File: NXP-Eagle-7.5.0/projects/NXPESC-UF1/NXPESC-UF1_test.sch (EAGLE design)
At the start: 2 parts, among them U1 MKV31F512VLL12-M, U2 MC34GD3000EP

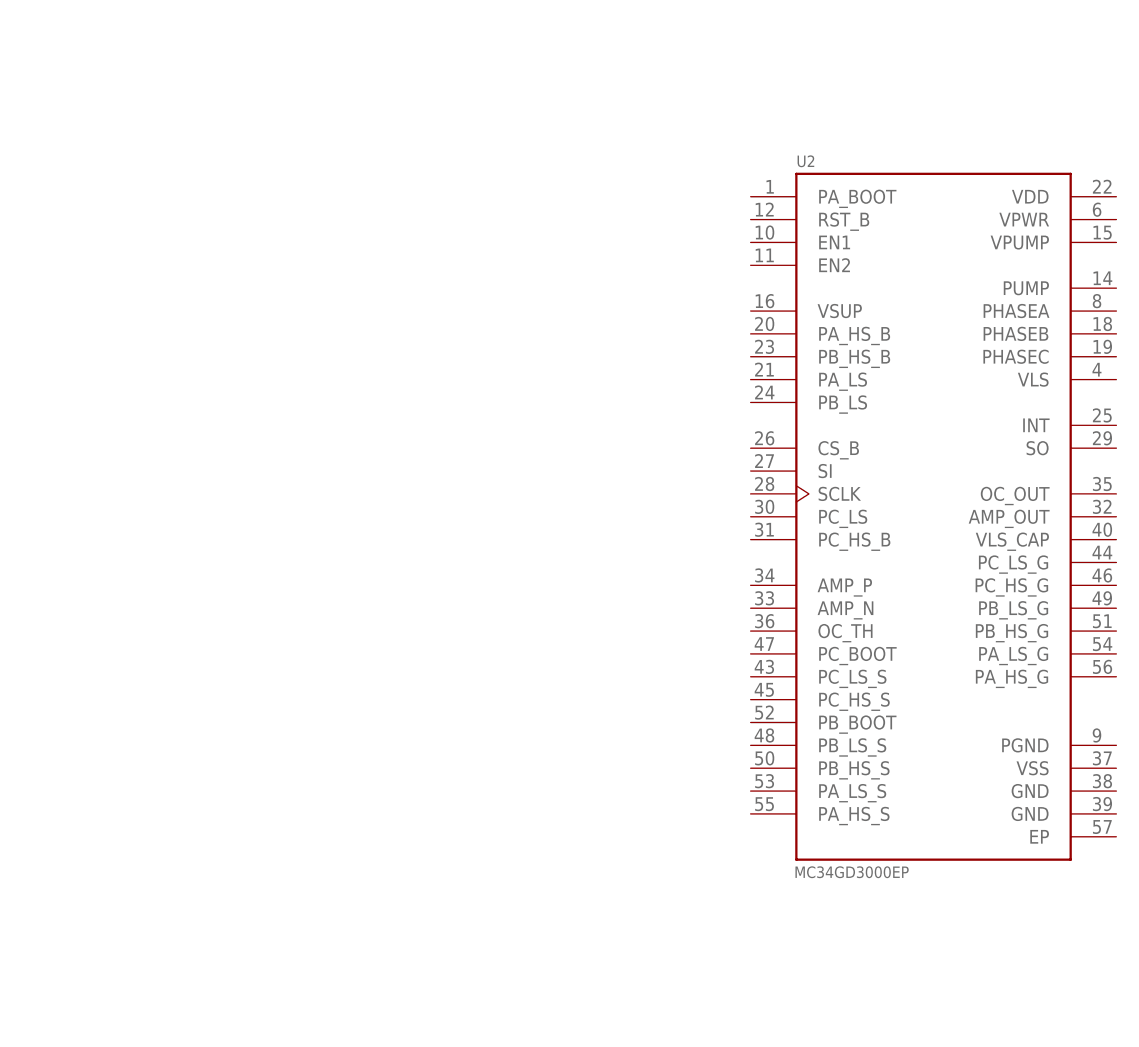
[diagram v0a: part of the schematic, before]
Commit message: Add FAN78888 device
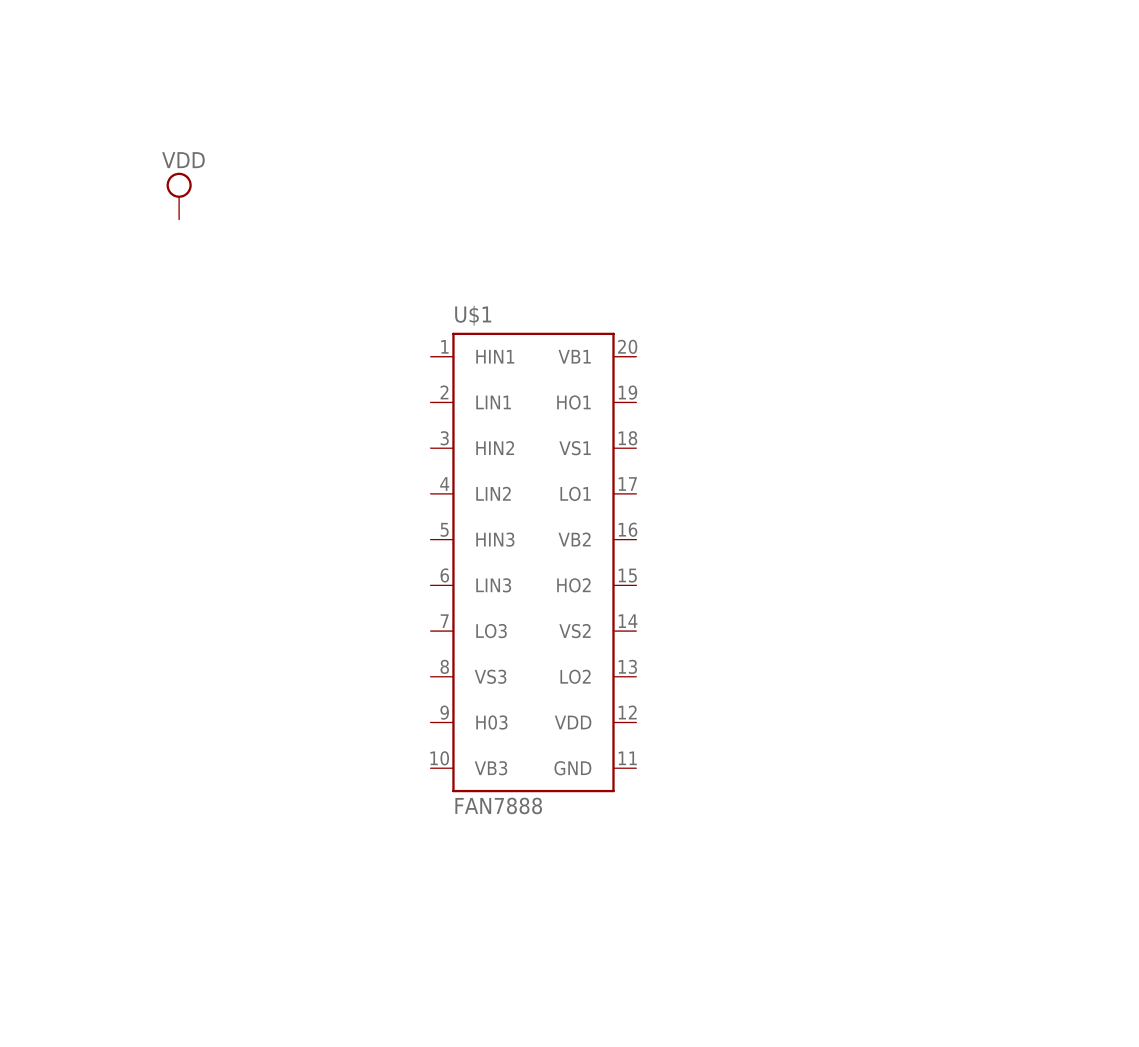
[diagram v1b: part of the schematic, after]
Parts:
- removed U2: MC34GD3000EP, MC34GD3000EP-None-Symbol-Eagle-1:MC34GD3000EP
- added U$1: FAN7888, FAN7888:FAN7888
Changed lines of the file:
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@@
 <?xml version="1.0" encoding="utf-8"?>
 <!DOCTYPE eagle SYSTEM "eagle.dtd">
-<eagle version="7.6.0">
+<eagle version="7.3.0">
 <drawing>
 <settings>
@@
 <parts>
 <part name="U1" library="MKV31F512VLL12" deviceset="MKV31F512VLL12" device="-M"/>
-<part name="U2" library="MC34GD3000EP-None-Symbol-Eagle-1" deviceset="MC34GD3000EP" device=""/>
+<part name="U$1" library="FAN7888" deviceset="FAN7888" device=""/>
+<part name="SUPPLY1" library="supply2" deviceset="VDD" device=""/>
 </parts>
 <sheets>
@@
 <instances>
 <instance part="U1" gate="G$1" x="15.24" y="78.74"/>
-<instance part="U2" gate="G$1" x="289.56" y="38.1"/>
+<instance part="U$1" gate="G$1" x="246.38" y="35.56"/>
+<instance part="SUPPLY1" gate="G$1" x="205.74" y="71.12"/>
 </instances>
 <busses>

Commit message: Begin sch
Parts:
- added C1: (no value), pixhawk2:CAP_POL1206
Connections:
- new net GND: U$1.GND
- new net N$5: U$1.HIN1, U1.PTC1/LLWU_P6
- new net N$6: U$1.LIN1, U1.PTC2
- new net N$7: U$1.HIN2, U1.PTC5/LLWU_P9
- new net N$8: U$1.LIN2, U1.PTC4/LLWU_P8
- new net VDD: C1.+, U$1.VDD
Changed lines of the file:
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@@
 <layer number="48" name="Document" color="7" fill="1" visible="no" active="no"/>
 <layer number="49" name="Reference" color="7" fill="1" visible="no" active="no"/>
+<layer number="50" name="dxf" color="7" fill="1" visible="no" active="no"/>
 <layer number="51" name="tDocu" color="7" fill="1" visible="no" active="no"/>
 <layer number="52" name="bDocu" color="7" fill="1" visible="no" active="no"/>
+<layer number="53" name="tGND_GNDA" color="7" fill="9" visible="no" active="no"/>
+<layer number="54" name="bGND_GNDA" color="1" fill="9" visible="no" active="no"/>
+<layer number="56" name="wert" color="7" fill="1" visible="no" active="no"/>
+<layer number="57" name="tCAD" color="12" fill="1" visible="no" active="no"/>
+<layer number="58" name="bCAD" color="9" fill="1" visible="no" active="no"/>
 <layer number="90" name="Modules" color="5" fill="1" visible="yes" active="yes"/>
 <layer number="91" name="Nets" color="2" fill="1" visible="yes" active="yes"/>
@@
 <layer number="97" name="Info" color="7" fill="1" visible="yes" active="yes"/>
 <layer number="98" name="Guide" color="6" fill="1" visible="yes" active="yes"/>
+<layer number="99" name="SpiceOrder" color="5" fill="1" visible="yes" active="yes"/>
+<layer number="100" name="Muster" color="7" fill="1" visible="no" active="no"/>
+<layer number="101" name="Patch_Top" color="12" fill="4" visible="yes" active="yes"/>
+<layer number="102" name="Vscore" color="7" fill="1" visible="yes" active="yes"/>
+<layer number="103" name="tMap" color="7" fill="1" visible="yes" active="yes"/>
+<layer number="104" name="Name" color="16" fill="1" visible="yes" active="yes"/>
+<layer number="105" name="tPlate" color="7" fill="1" visible="yes" active="yes"/>
+<layer number="106" name="bPlate" color="7" fill="1" visible="yes" active="yes"/>
+<layer number="107" name="Crop" color="7" fill="1" visible="yes" active="yes"/>
+<layer number="108" name="fp8" color="7" fill="1" visible="yes" active="yes"/>
+<layer number="109" name="fp9" color="7" fill="1" visible="yes" active="yes"/>
+<layer number="110" name="fp0" color="7" fill="1" visible="yes" active="yes"/>
+<layer number="111" name="LPC17xx" color="7" fill="1" visible="yes" active="yes"/>
+<layer number="112" name="tSilk" color="7" fill="1" visible="yes" active="yes"/>
+<layer number="116" name="Patch_BOT" color="9" fill="4" visible="yes" active="yes"/>
+<layer number="121" name="_tsilk" color="7" fill="1" visible="yes" active="yes"/>
+<layer number="122" name="_bsilk" color="7" fill="1" visible="yes" active="yes"/>
+<layer number="123" name="tTestmark" color="7" fill="1" visible="yes" active="yes"/>
+<layer number="124" name="bTestmark" color="7" fill="1" visible="yes" active="yes"/>
+<layer number="125" name="_tNames" color="7" fill="1" visible="yes" active="yes"/>
+<layer number="126" name="_bnames" color="7" fill="1" visible="yes" active="yes"/>
+<layer number="127" name="_tvalues" color="7" fill="1" visible="yes" active="yes"/>
+<layer number="128" name="_bvalues" color="7" fill="1" visible="yes" active="yes"/>
+<layer number="131" name="tAdjust" color="7" fill="1" visible="yes" active="yes"/>
+<layer number="132" name="bAdjust" color="7" fill="1" visible="yes" active="yes"/>
+<layer number="144" name="Drill_legend" color="7" fill="1" visible="yes" active="yes"/>
+<layer number="150" name="Notes" color="7" fill="1" visible="yes" active="yes"/>
+<layer number="151" name="HeatSink" color="7" fill="1" visible="yes" active="yes"/>
+<layer number="152" name="_bDocu" color="7" fill="1" visible="yes" active="yes"/>
+<layer number="153" name="FabDoc1" color="6" fill="1" visible="no" active="no"/>
+<layer number="154" name="FabDoc2" color="2" fill="1" visible="no" active="no"/>
+<layer number="155" name="FabDoc3" color="7" fill="15" visible="no" active="no"/>
+<layer number="199" name="Contour" color="7" fill="1" visible="yes" active="yes"/>
+<layer number="200" name="200bmp" color="1" fill="10" visible="yes" active="yes"/>
+<layer number="201" name="201bmp" color="2" fill="10" visible="yes" active="yes"/>
+<layer number="202" name="202bmp" color="3" fill="10" visible="yes" active="yes"/>
+<layer number="203" name="203bmp" color="4" fill="10" visible="yes" active="yes"/>
+<layer number="204" name="204bmp" color="5" fill="10" visible="yes" active="yes"/>
+<layer number="205" name="205bmp" color="6" fill="10" visible="yes" active="yes"/>
+<layer number="206" name="206bmp" color="7" fill="10" visible="yes" active="yes"/>
+<layer number="207" name="207bmp" color="8" fill="10" visible="yes" active="yes"/>
+<layer number="208" name="208bmp" color="9" fill="10" visible="yes" active="yes"/>
+<layer number="209" name="209bmp" color="7" fill="1" visible="yes" active="yes"/>
+<layer number="210" name="210bmp" color="7" fill="1" visible="yes" active="yes"/>
+<layer number="211" name="211bmp" color="7" fill="1" visible="yes" active="yes"/>
+<layer number="212" name="212bmp" color="7" fill="1" visible="yes" active="yes"/>
+<layer number="213" name="213bmp" color="7" fill="1" visible="yes" active="yes"/>
+<layer number="214" name="214bmp" color="7" fill="1" visible="yes" active="yes"/>
+<layer number="215" name="215bmp" color="7" fill="1" visible="yes" active="yes"/>
+<layer number="216" name="216bmp" color="7" fill="1" visible="yes" active="yes"/>
+<layer number="217" name="217bmp" color="18" fill="1" visible="no" active="no"/>
+<layer number="218" name="218bmp" color="19" fill="1" visible="no" active="no"/>
+<layer number="219" name="219bmp" color="20" fill="1" visible="no" active="no"/>
+<layer number="220" name="220bmp" color="21" fill="1" visible="no" active="no"/>
+<layer number="221" name="221bmp" color="22" fill="1" visible="no" active="no"/>
+<layer number="222" name="222bmp" color="23" fill="1" visible="no" active="no"/>
+<layer number="223" name="223bmp" color="24" fill="1" visible="no" active="no"/>
+<layer number="224" name="224bmp" color="25" fill="1" visible="no" active="no"/>
+<layer number="231" name="Eagle3D_PG1" color="14" fill="1" visible="yes" active="yes"/>
+<layer number="232" name="Eagle3D_PG2" color="14" fill="2" visible="yes" active="yes"/>
+<layer number="233" name="Eagle3D_PG3" color="14" fill="4" visible="yes" active="yes"/>
+<layer number="248" name="Housing" color="7" fill="1" visible="yes" active="yes"/>
+<layer number="249" name="Edge" color="7" fill="1" visible="yes" active="yes"/>
+<layer number="250" name="Descript" color="3" fill="1" visible="no" active="no"/>
+<layer number="251" name="SMDround" color="12" fill="11" visible="no" active="no"/>
+<layer number="254" name="cooling" color="7" fill="1" visible="yes" active="yes"/>
 </layers>
 <schematic xreflabel="%F%N/%S" xrefpart="/%S.%C%R">
@@
 <part name="U$1" library="FAN7888" deviceset="FAN7888" device=""/>
 <part name="SUPPLY1" library="supply2" deviceset="VDD" device=""/>
+<part name="SUPPLY2" library="supply2" deviceset="GND" device=""/>
+<part name="C1" library="pixhawk2" deviceset="CAP_POL" device="1206"/>
 </parts>
 <sheets>
@@
 <instance part="U1" gate="G$1" x="15.24" y="78.74"/>
 <instance part="U$1" gate="G$1" x="246.38" y="35.56"/>
-<instance part="SUPPLY1" gate="G$1" x="205.74" y="71.12"/>
+<instance part="SUPPLY1" gate="G$1" x="276.86" y="20.32"/>
+<instance part="SUPPLY2" gate="GND" x="276.86" y="0"/>
+<instance part="C1" gate="G$1" x="276.86" y="12.7"/>
 </instances>
 <busses>
 </busses>
 <nets>
+<net name="VDD" class="0">
+<segment>
+<pinref part="SUPPLY1" gate="G$1" pin="VDD"/>
+<pinref part="U$1" gate="G$1" pin="VDD"/>
+<wire x1="276.86" y1="17.78" x2="269.24" y2="17.78" width="0.1524" layer="91"/>
+<wire x1="269.24" y1="17.78" x2="269.24" y2="12.7" width="0.1524" layer="91"/>
+<wire x1="269.24" y1="12.7" x2="256.54" y2="12.7" width="0.1524" layer="91"/>
+<pinref part="C1" gate="G$1" pin="+"/>
+<wire x1="276.86" y1="15.24" x2="276.86" y2="17.78" width="0.1524" layer="91"/>
+</segment>
+</net>
+<net name="GND" class="0">
+<segment>
+<pinref part="U$1" gate="G$1" pin="GND"/>
+<pinref part="SUPPLY2" gate="GND" pin="GND"/>
+<wire x1="256.54" y1="7.62" x2="276.86" y2="7.62" width="0.1524" layer="91"/>
+<wire x1="276.86" y1="7.62" x2="276.86" y2="2.54" width="0.1524" layer="91"/>
+</segment>
+</net>
+<net name="N$5" class="0">
+<segment>
+<pinref part="U1" gate="G$1" pin="PTC1/LLWU_P6"/>
+<wire x1="167.64" y1="5.08" x2="200.66" y2="5.08" width="0.1524" layer="91"/>
+<wire x1="200.66" y1="5.08" x2="200.66" y2="53.34" width="0.1524" layer="91"/>
+<wire x1="200.66" y1="53.34" x2="233.68" y2="53.34" width="0.1524" layer="91"/>
+<pinref part="U$1" gate="G$1" pin="HIN1"/>
+</segment>
+</net>
+<net name="N$6" class="0">
+<segment>
+<pinref part="U1" gate="G$1" pin="PTC2"/>
+<wire x1="167.64" y1="7.62" x2="203.2" y2="7.62" width="0.1524" layer="91"/>
+<wire x1="203.2" y1="7.62" x2="203.2" y2="48.26" width="0.1524" layer="91"/>
+<pinref part="U$1" gate="G$1" pin="LIN1"/>
+<wire x1="203.2" y1="48.26" x2="233.68" y2="48.26" width="0.1524" layer="91"/>
+</segment>
+</net>
+<net name="N$7" class="0">
+<segment>
+<wire x1="205.74" y1="43.18" x2="205.74" y2="20.32" width="0.1524" layer="91"/>
+<pinref part="U1" gate="G$1" pin="PTC5/LLWU_P9"/>
+<wire x1="205.74" y1="20.32" x2="167.64" y2="20.32" width="0.1524" layer="91"/>
+<pinref part="U$1" gate="G$1" pin="HIN2"/>
+<wire x1="205.74" y1="43.18" x2="233.68" y2="43.18" width="0.1524" layer="91"/>
+</segment>
+</net>
+<net name="N$8" class="0">
+<segment>
+<wire x1="208.28" y1="38.1" x2="208.28" y2="17.78" width="0.1524" layer="91"/>
+<pinref part="U1" gate="G$1" pin="PTC4/LLWU_P8"/>
+<wire x1="208.28" y1="17.78" x2="167.64" y2="17.78" width="0.1524" layer="91"/>
+<pinref part="U$1" gate="G$1" pin="LIN2"/>
+<wire x1="208.28" y1="38.1" x2="233.68" y2="38.1" width="0.1524" layer="91"/>
+</segment>
+</net>
 </nets>
 </sheet>

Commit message: Adding library and datasheet parts
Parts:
- added J1: FLH1-03SZ-S3A-T, etc-connector-003a:FLH1-03SZ-S3A-T
- added R1, R2, R4, R5, R6, R7: RESC0603-200R-1, etc-rcl:RESC0603-200R-1
- added TP1: (no value), etc-connector-003a:TP-TH-SMLL
- added U2, U3, U4, U5, U6, U7: PSMN1R4-30YLD, PSMN1R2-25YL_115:PSMN1R4-30YLD
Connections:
- new net HOA: R2.1, U$1.HO1
- new net HOB: R4.1, U$1.HO2
- new net HOC: R6.1, U$1.H03
- new net LOA: R1.1, U$1.LO1
- new net LOB: R5.1, U$1.LO2
- new net LOC: R7.1, U$1.LO3
- new net N$11: R2.2, U2.G
- new net N$12: R1.2, U3.G
- new net N$13: R4.2, U4.G
- new net N$14: R5.2, U5.G
- new net N$15: R6.2, U6.G
- new net N$16: R7.2, U7.G
- new net N$2: TP1.1, U2.D, U4.D, U6.D
- new net PH_A: J1.1, U$1.VS1, U2.S, U3.D
- new net PH_B: J1.2, U$1.VS2, U4.S, U5.D
- new net PH_C: J1.3, U$1.VS3, U6.S, U7.D
- net GND: now also C1.-
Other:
- note added: "MOTOR OUTPUT"
- moved on the sheet: C1
